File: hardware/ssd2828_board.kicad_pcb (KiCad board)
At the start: 4 copper layers, 91.3 x 35.4 mm, 124 parts, among them IC1 TLV62568DBVR, IC2 MIC5501-3.0YM5-TR, IC3 TPS65131TRGERQ1, J1 FH35C-25S-0.3SHW_50_, J2 FH35C-25S-0.3SHW_50_, J3 Conn_01x34, J4 245863050104829+, J5 503548-1220, J8 FH35C-25S-0.3SHW_50_, U1 SSD2828QN4, U2 PAM2306DYPAA, U3 MIC3289, U4 LP3320, Y1 24mhz

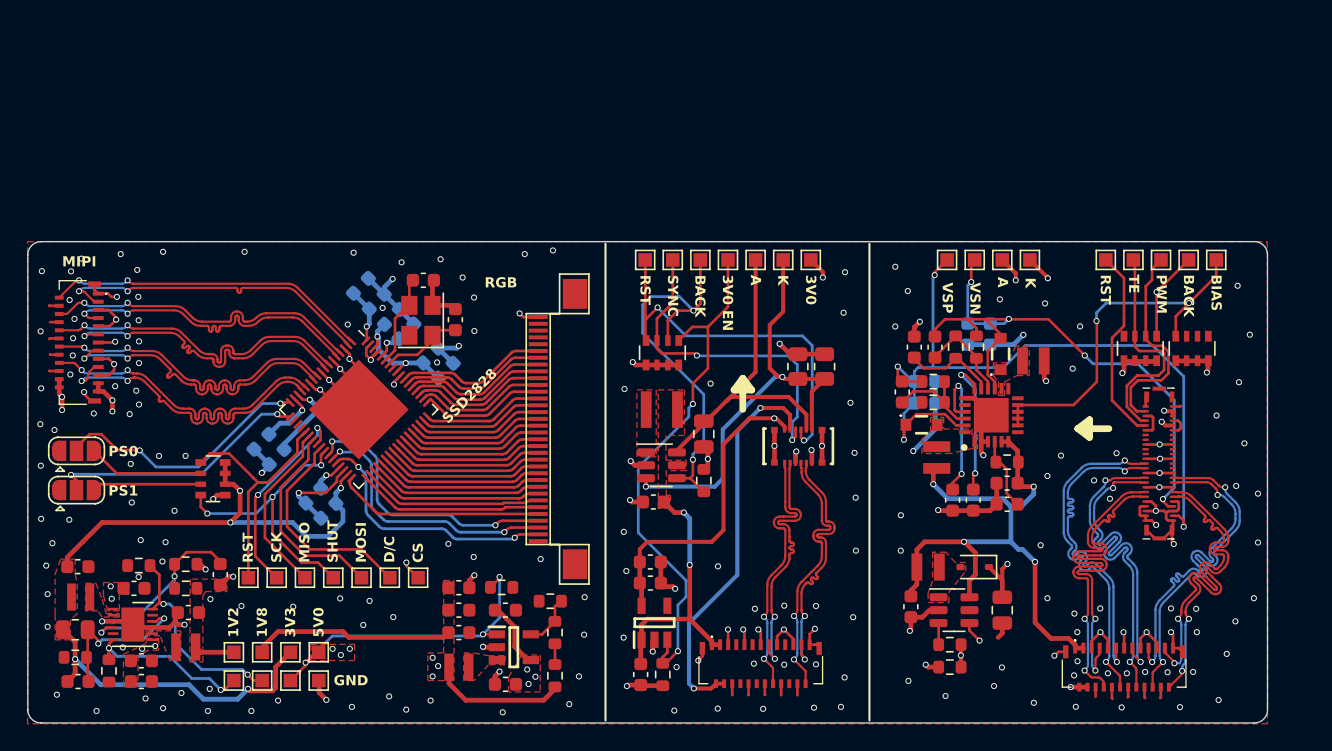
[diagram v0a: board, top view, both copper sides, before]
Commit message: fixed some intra-pair skew errors and filleted some lanes
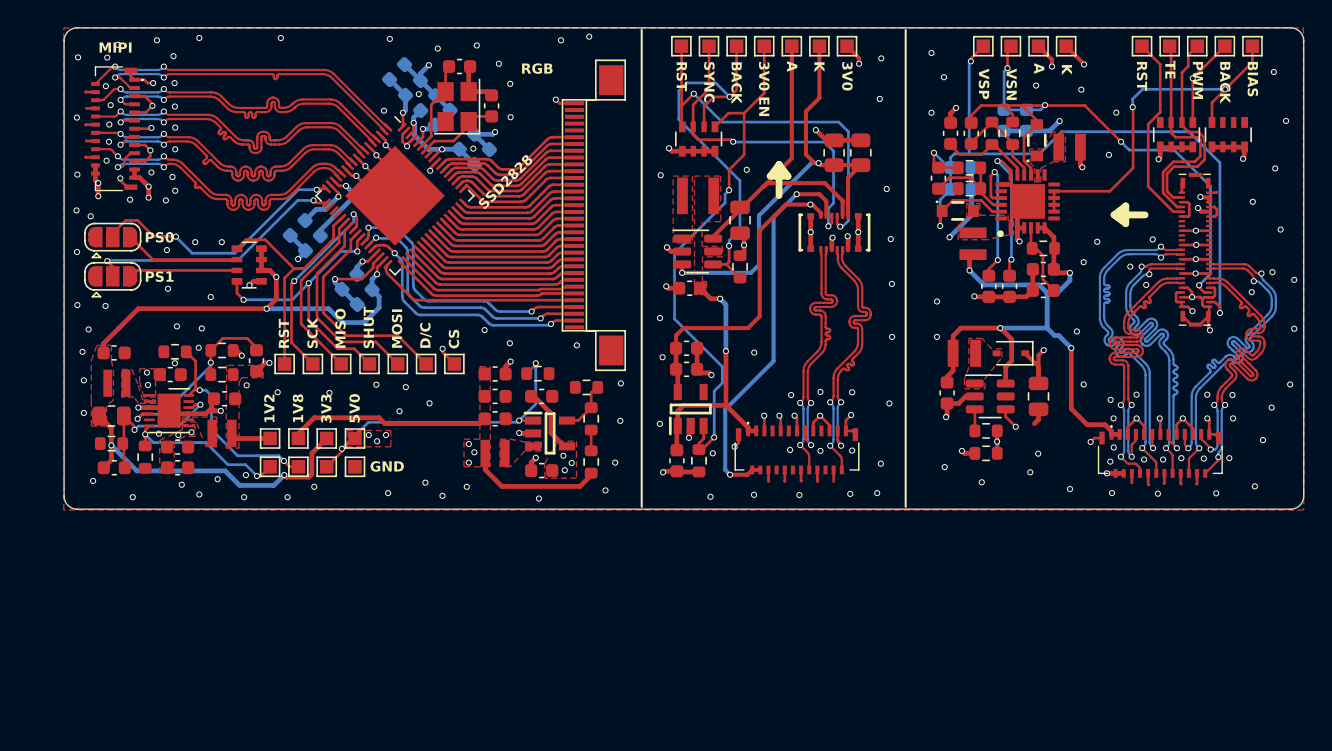
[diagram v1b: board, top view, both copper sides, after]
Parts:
- moved D1 16.0 mm to (121.4, 75.1)
- moved IC2 16.0 mm to (97.8, 79.2)
- moved J3 16.0 mm to (89.3, 64.9)
- moved J5 16.0 mm to (108.4, 66.2)
- moved L1 16.0 mm to (63.3, 81.0)
- moved L3 16.0 mm to (83.4, 82.4)
- moved L7 16.0 mm to (118.0, 75.1)
- moved R23 16.0 mm to (119.6, 82.4)
- moved R4 16.0 mm to (55.2, 81.7)
- moved RN1 16.0 mm to (65.3, 68.6)
- moved TP10 16.0 mm to (69.0, 83.4)
- moved TP11 16.0 mm to (66.9, 83.4)
- moved TP12 16.0 mm to (71.0, 83.4)
- moved TP21 16.0 mm to (73.1, 83.4)
- moved U2 16.0 mm to (59.4, 79.3)
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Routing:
- net GND: track 185.6 -> 183.9 mm, vias 219 -> 218
- net /VS035ZSM/MIPI_CLK_N: track 24.0 -> 25.2 mm

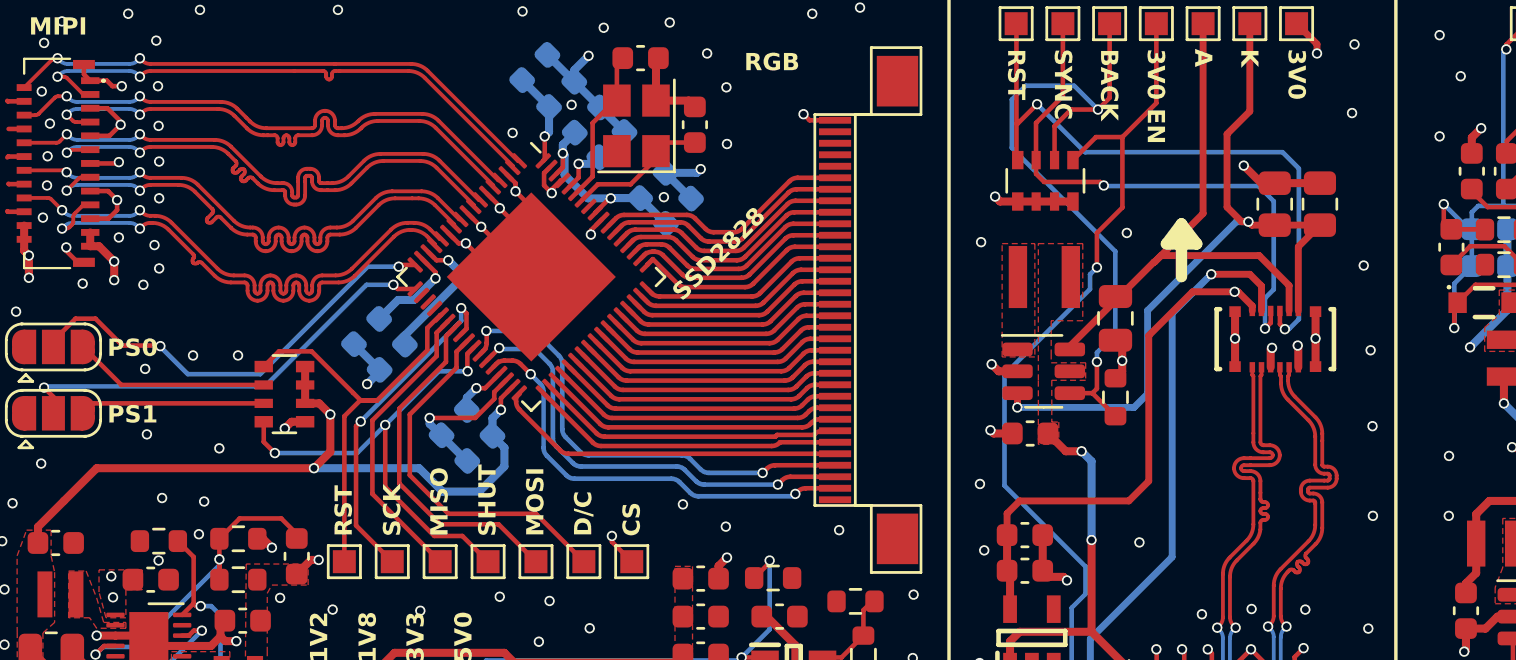
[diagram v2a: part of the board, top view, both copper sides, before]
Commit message: tweaked some MIPI traces on the SSD2828 board
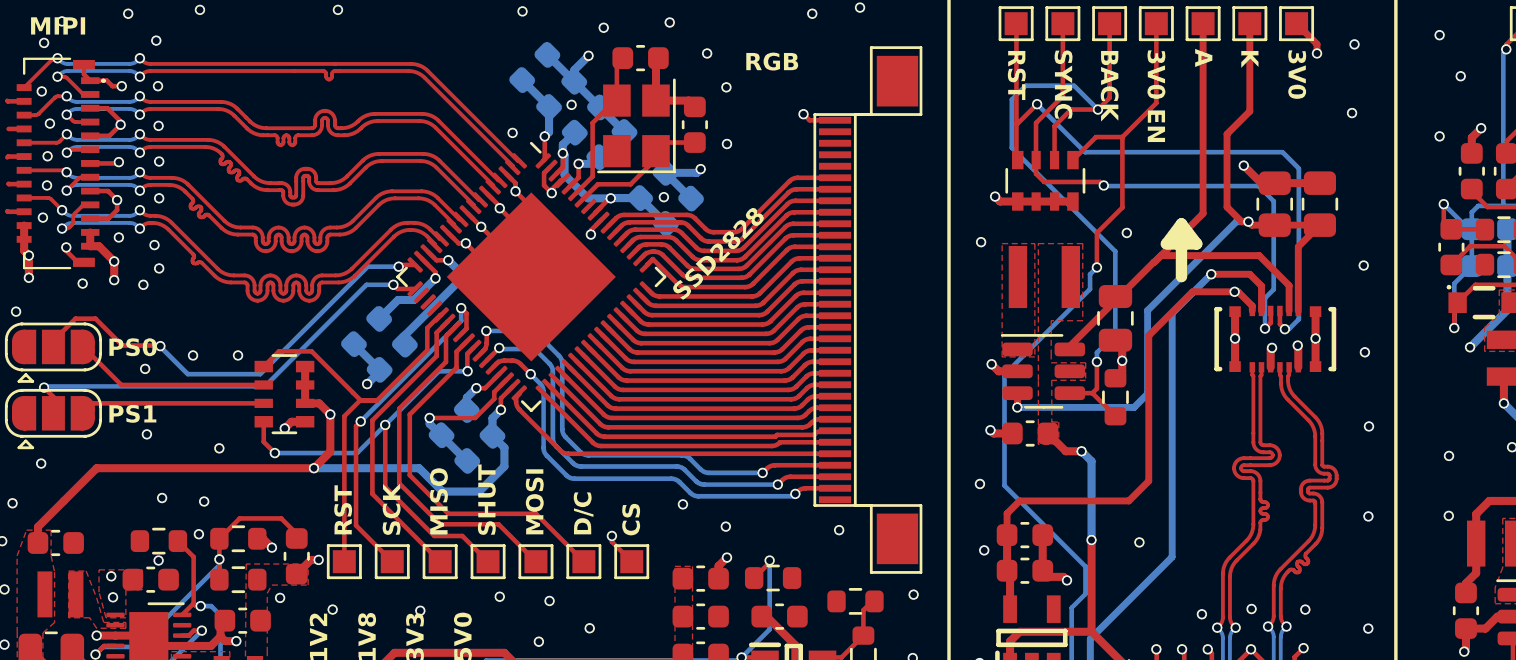
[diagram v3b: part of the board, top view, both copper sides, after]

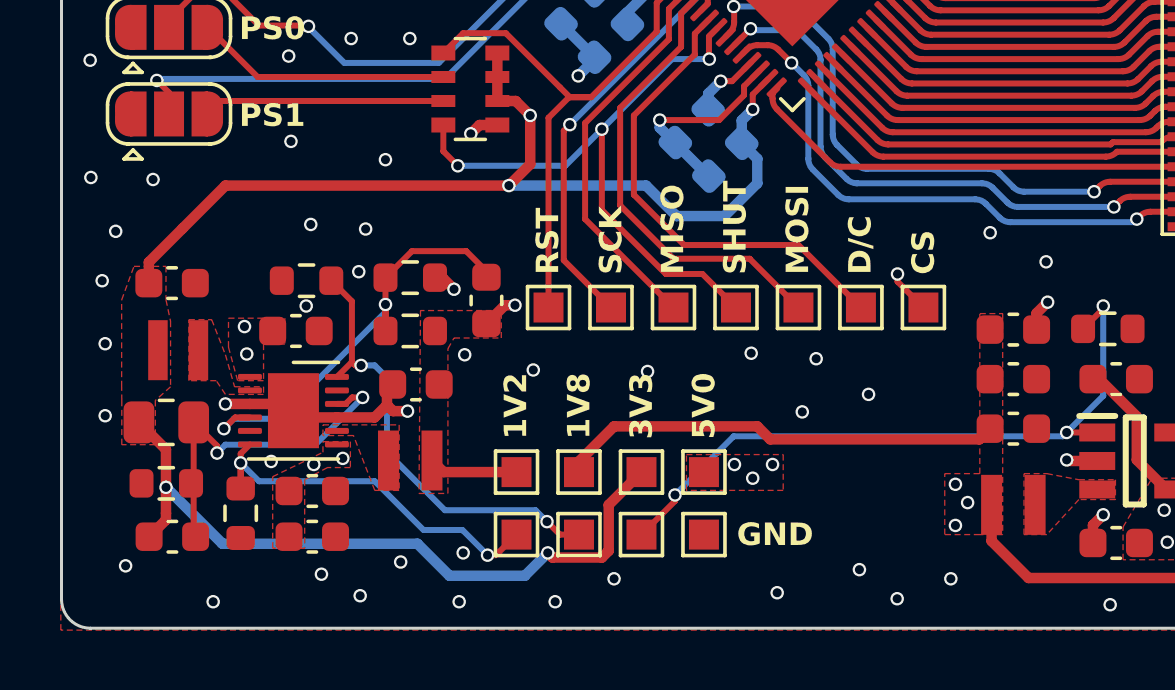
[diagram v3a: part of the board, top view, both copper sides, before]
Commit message: added solder bridges on all the generated voltage rails on the SSD2828 board
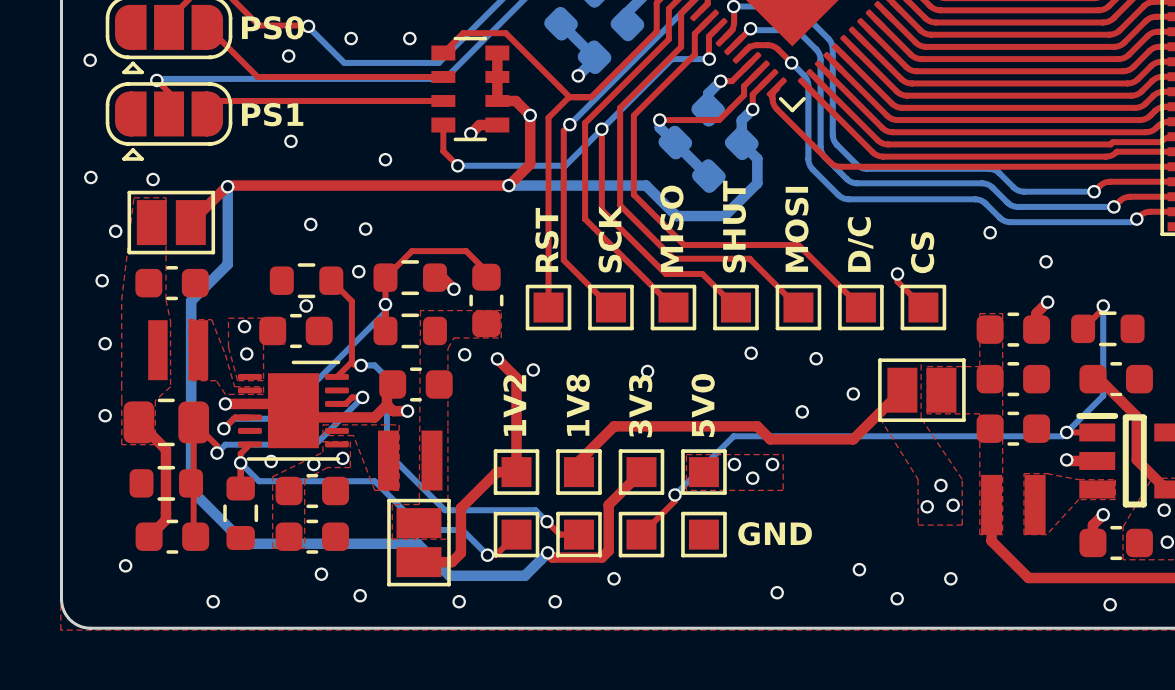
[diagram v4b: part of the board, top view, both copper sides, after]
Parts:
- added JP3: SolderJumper_2_Open, Jumper:SolderJumper-2_P1.3mm_Open_Pad1.0x1.5mm, F.Cu at (80.4, 78.6)
- added JP4: SolderJumper_2_Open, Jumper:SolderJumper-2_P1.3mm_Open_Pad1.0x1.5mm, F.Cu at (55.4, 73.0)
- added JP5: SolderJumper_2_Open, Jumper:SolderJumper-2_P1.3mm_Open_Pad1.0x1.5mm, F.Cu at (63.6, 83.7)
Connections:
- C16 pad 1: +1V2 -> Net-(JP5-A)
- C17 pad 1: +3V3 -> Net-(JP4-A)
- C18 pad 1: +1V2 -> Net-(JP5-A)
- C19 pad 1: +3V3 -> Net-(JP4-A)
- C20 pad 1: +1V8 -> Net-(JP3-A)
- C21 pad 1: +1V8 -> Net-(JP3-A)
- C22 pad 1: +1V8 -> Net-(JP3-A)
- L1 pad 2: +1V2 -> Net-(JP5-A)
- L2 pad 2: +3V3 -> Net-(JP4-A)
- L3 pad 2: +1V8 -> Net-(JP3-A)
- R1 pad 1: +1V2 -> Net-(JP5-A)
- R2 pad 1: +3V3 -> Net-(JP4-A)
- R8 pad 1: +1V8 -> Net-(JP3-A)
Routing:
- net +1V8: track 95.7 -> 83.2 mm
- net Net-(JP3-A): track 0.00 -> 10.1 mm
- net +1V2: track 50.3 -> 57.5 mm
- net Net-(JP4-A): track 0.00 -> 4.42 mm
- net +3V3: track 85.9 -> 88.6 mm
- net GND: vias 218 -> 216
- added copper zone on F.Cu, net Net-(JP3-A)
- added copper zone on F.Cu, net Net-(JP4-A)
- added copper zone on F.Cu, net Net-(JP5-A)
- removed copper zone on F.Cu, net +1V2
- removed copper zone on F.Cu, net +3V3

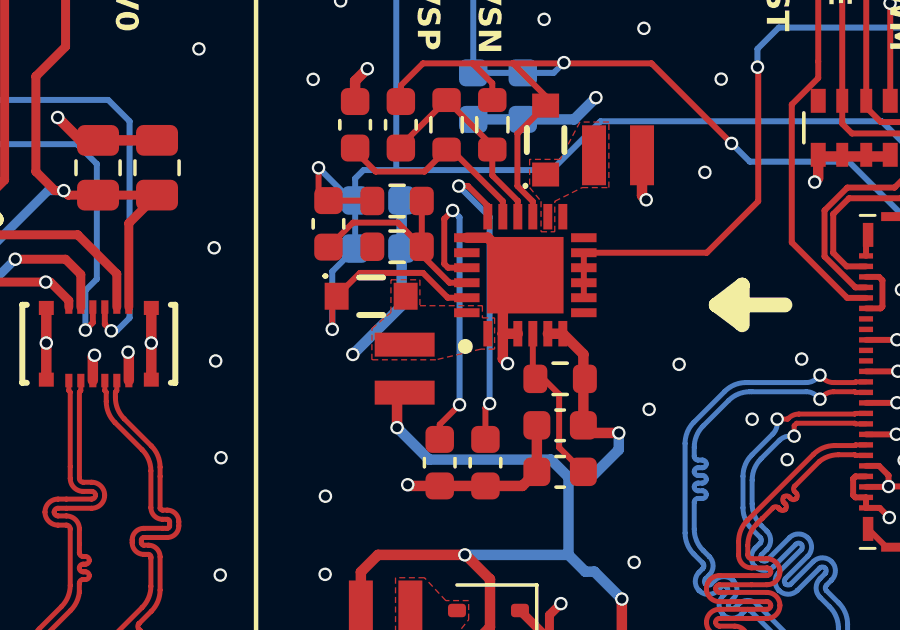
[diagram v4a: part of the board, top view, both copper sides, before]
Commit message: updated tps6513 footprint to vqfn24 + fixed some missing connections near it
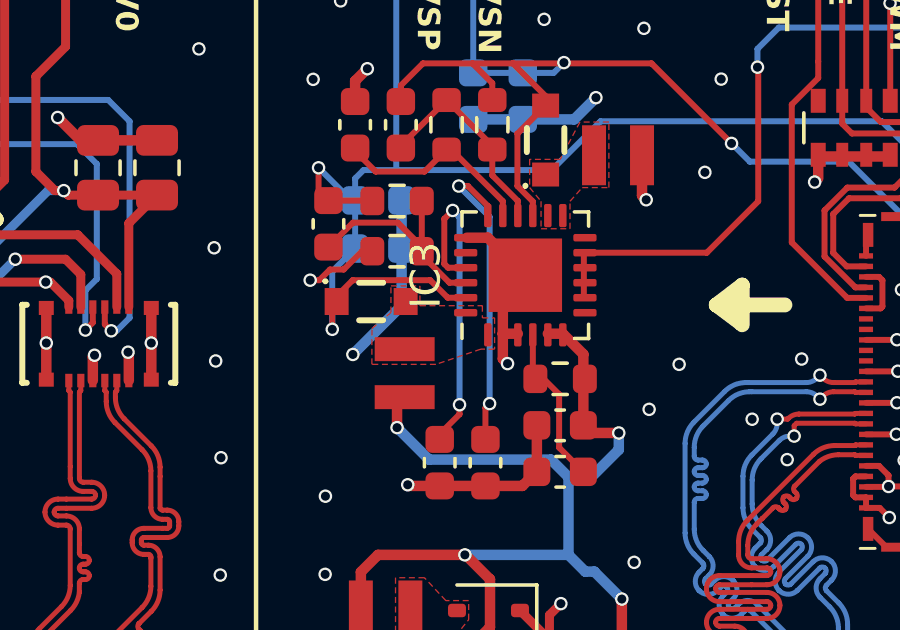
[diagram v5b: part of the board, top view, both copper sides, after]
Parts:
- IC3: footprint SamacSys_Parts:QFN50P400X400X100-25N-D -> Package_DFN_QFN:VQFN-24-1EP_4x4mm_P0.5mm_EP2.45x2.45mm
- moved D3 0.18 mm to (117.5, 64.8)
- moved L5 0.15 mm to (118.6, 67.2)
- moved R17 0.15 mm to (118.4, 63.1)
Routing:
- net GND: track 183.9 -> 186.4 mm, vias 216 -> 217
